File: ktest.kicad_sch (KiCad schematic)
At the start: 2 parts

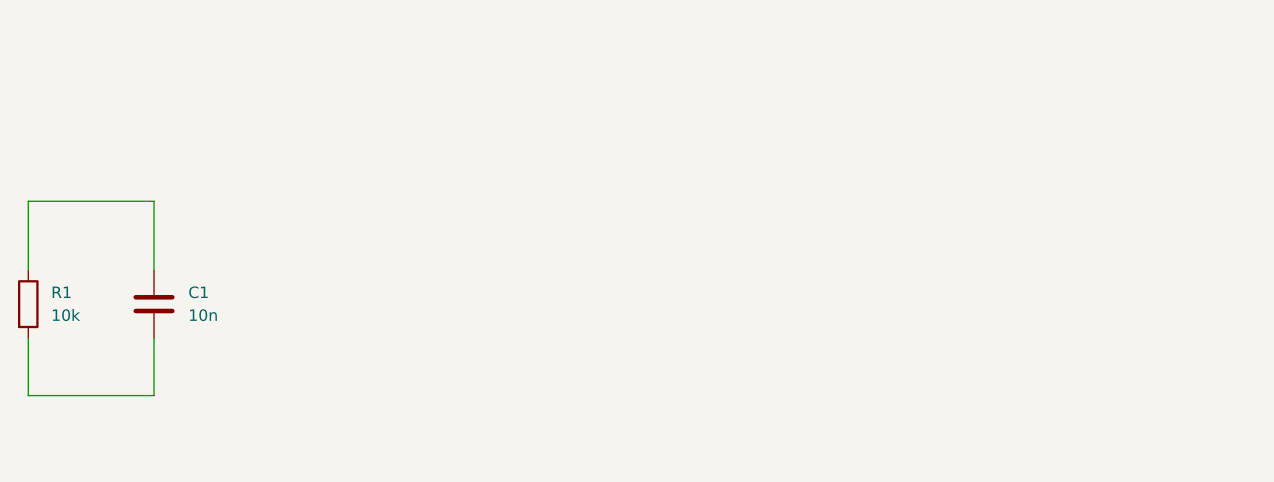
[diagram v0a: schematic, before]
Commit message: 4 layers
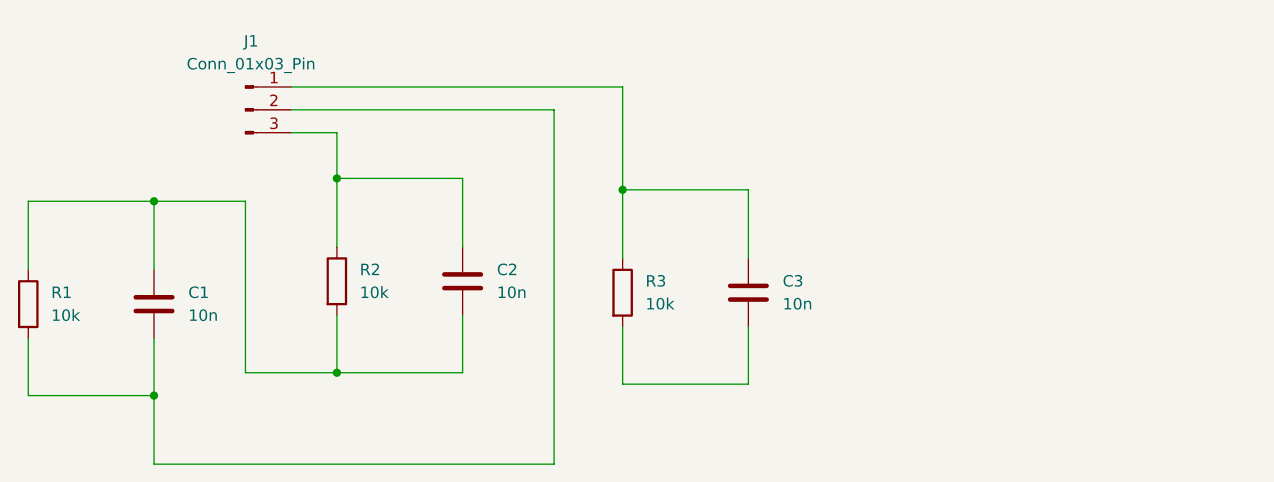
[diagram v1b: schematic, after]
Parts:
- added C2, C3: 10n, Capacitor_SMD:CP_Elec_5x5.9, symbol Device:C
- added J1: Conn_01x03_Pin, Connector_PinSocket_2.54mm:PinSocket_1x03_P2.54mm_Vertical, symbol Connector:Conn_01x03_Pin
- added R2, R3: 10k, Resistor_SMD:R_01005_0402Metric, symbol Device:R
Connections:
- net at C1.1, R1.1: now also C2.2, R2.2
- net at C1.2, R1.2: now also J1.2 (Pin_2)
- new net: C2.1, J1.3 (Pin_3), R2.1
- new net: C3.1, J1.1 (Pin_1), R3.1
- new net: C3.2, R3.2

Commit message: updating sheet templates
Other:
- company: (none) -> Example company
- title: (none) -> Kibot test

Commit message: fab and assy docs update
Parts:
- added H1, H2: MountingHole, MountingHole:MountingHole_3.2mm_M3, symbol Mechanical:MountingHole
- added H3: MountingHole, MountingHole:MountingHole_2.7mm_M2.5, symbol Mechanical:MountingHole
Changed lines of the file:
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@@
+	)
+	(symbol
+		(lib_id "Mechanical:MountingHole")
+		(at 194.31 106.68 0)
+		(unit 1)
+		(body_style 1)
+		(exclude_from_sim no)
+		(in_bom no)
+		(on_board yes)
+		(in_pos_files yes)
+		(dnp no)
+		(fields_autoplaced yes)
+		(property "Reference" "H2"
+			(at 196.85 105.4099 0)
+			(show_name no)
+			(do_not_autoplace no)
+			(effects
+				(font
+					(size 1.27 1.27)
+				)
+				(justify left)
+			)
+		)
+		(property "Value" "MountingHole"
+			(at 196.85 107.9499 0)
+			(show_name no)
+			(do_not_autoplace no)
+			(effects
+				(font
+					(size 1.27 1.27)
+				)
+				(justify left)
+			)
+		)
+		(property "Footprint" "MountingHole:MountingHole_3.2mm_M3"
+			(at 194.31 106.68 0)
+			(hide yes)
+			(show_name no)
+			(do_not_autoplace no)
+			(effects
+				(font
+					(size 1.27 1.27)
+				)
+			)
+		)
+		(property "Datasheet" ""
+			(at 194.31 106.68 0)
+			(hide yes)
+			(show_name no)
+			(do_not_autoplace no)
+			(effects
+				(font
+					(size 1.27 1.27)
+				)
+			)
+		)
+		(property "Description" "Mounting Hole without connection"
+			(at 194.31 106.68 0)
+			(hide yes)
+			(show_name no)
+			(do_not_autoplace no)
+			(effects
+				(font
+					(size 1.27 1.27)
+				)
+			)
+		)
+		(instances
+			(project "ktest"
+				(path "/f14ff7c3-fe34-4697-84b8-3cc06a5a3565"
+					(reference "H2")
+					(unit 1)
+				)
+			)
+		)
 	)
 	(symbol
@@
 	)
 	(symbol
+		(lib_id "Mechanical:MountingHole")
+		(at 194.31 97.79 0)
+		(unit 1)
+		(body_style 1)
+		(exclude_from_sim no)
+		(in_bom no)
+		(on_board yes)
+		(in_pos_files yes)
+		(dnp no)
+		(fields_autoplaced yes)
+		(property "Reference" "H1"
+			(at 196.85 96.5199 0)
+			(show_name no)
+			(do_not_autoplace no)
+			(effects
+				(font
+					(size 1.27 1.27)
+				)
+				(justify left)
+			)
+		)
+		(property "Value" "MountingHole"
+			(at 196.85 99.0599 0)
+			(show_name no)
+			(do_not_autoplace no)
+			(effects
+				(font
+					(size 1.27 1.27)
+				)
+				(justify left)
+			)
+		)
+		(property "Footprint" "MountingHole:MountingHole_3.2mm_M3"
+			(at 194.31 97.79 0)
+			(hide yes)
+			(show_name no)
+			(do_not_autoplace no)
+			(effects
+				(font
+					(size 1.27 1.27)
+				)
+			)
+		)
+		(property "Datasheet" ""
+			(at 194.31 97.79 0)
+			(hide yes)
+			(show_name no)
+			(do_not_autoplace no)
+			(effects
+				(font
+					(size 1.27 1.27)
+				)
+			)
+		)
+		(property "Description" "Mounting Hole without connection"
+			(at 194.31 97.79 0)
+			(hide yes)
+			(show_name no)
+			(do_not_autoplace no)
+			(effects
+				(font
+					(size 1.27 1.27)
+				)
+			)
+		)
+		(instances
+			(project "ktest"
+				(path "/f14ff7c3-fe34-4697-84b8-3cc06a5a3565"
+					(reference "H1")
+					(unit 1)
+				)
+			)
+		)
+	)
+	(symbol
 		(lib_id "Device:R")
 		(at 76.2 101.6 0)
@@
 					(unit 1)
 				)
+			)
+		)
+	)
+	(symbol
+		(lib_id "Mechanical:MountingHole")
+		(at 194.31 114.3 0)
+		(unit 1)
+		(body_style 1)
+		(exclude_from_sim no)
+		(in_bom no)
+		(on_board yes)
+		(in_pos_files yes)
+		(dnp no)
+		(fields_autoplaced yes)
+		(property "Reference" "H3"
+			(at 196.85 113.0299 0)
+			(show_name no)
+			(do_not_autoplace no)
+			(effects
+				(font
+					(size 1.27 1.27)
+				)
+				(justify left)
+			)
+		)
+		(property "Value" "MountingHole"
+			(at 196.85 115.5699 0)
+			(show_name no)
+			(do_not_autoplace no)
+			(effects
+				(font
+					(size 1.27 1.27)
+				)
+				(justify left)
+			)
+		)
+		(property "Footprint" "MountingHole:MountingHole_2.7mm_M2.5"
+			(at 194.31 114.3 0)
+			(hide yes)
+			(show_name no)
+			(do_not_autoplace no)
+			(effects
+				(font
+					(size 1.27 1.27)
+				)
+			)
+		)
+		(property "Datasheet" ""
+			(at 194.31 114.3 0)
+			(hide yes)
+			(show_name no)
+			(do_not_autoplace no)
+			(effects
+				(font
+					(size 1.27 1.27)
+				)
+			)
+		)
+		(property "Description" "Mounting Hole without connection"
+			(at 194.31 114.3 0)
+			(hide yes)
+			(show_name no)
+			(do_not_autoplace no)
+			(effects
+				(font
+					(size 1.27 1.27)
+				)
+			)
+		)
+		(instances
+			(project "ktest"
+				(path "/f14ff7c3-fe34-4697-84b8-3cc06a5a3565"
+					(reference "H3")
+					(unit 1)
+				)

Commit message: extra light source
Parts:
- added D1: LED, LED_THT:LED_D1.8mm_W3.3mm_H2.4mm, symbol Device:LED
- added R4, R5: 10k, Resistor_THT:R_Axial_DIN0414_L11.9mm_D4.5mm_P5.08mm_Vertical, symbol Device:R
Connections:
- net at C3.1, J1.1 (Pin_1), R3.1: now also D1.1 (K)
- new net: D1.2 (A), R4.1, R5.1
- new net: R4.2, R5.2
